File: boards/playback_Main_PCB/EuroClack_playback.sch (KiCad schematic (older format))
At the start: 31 parts

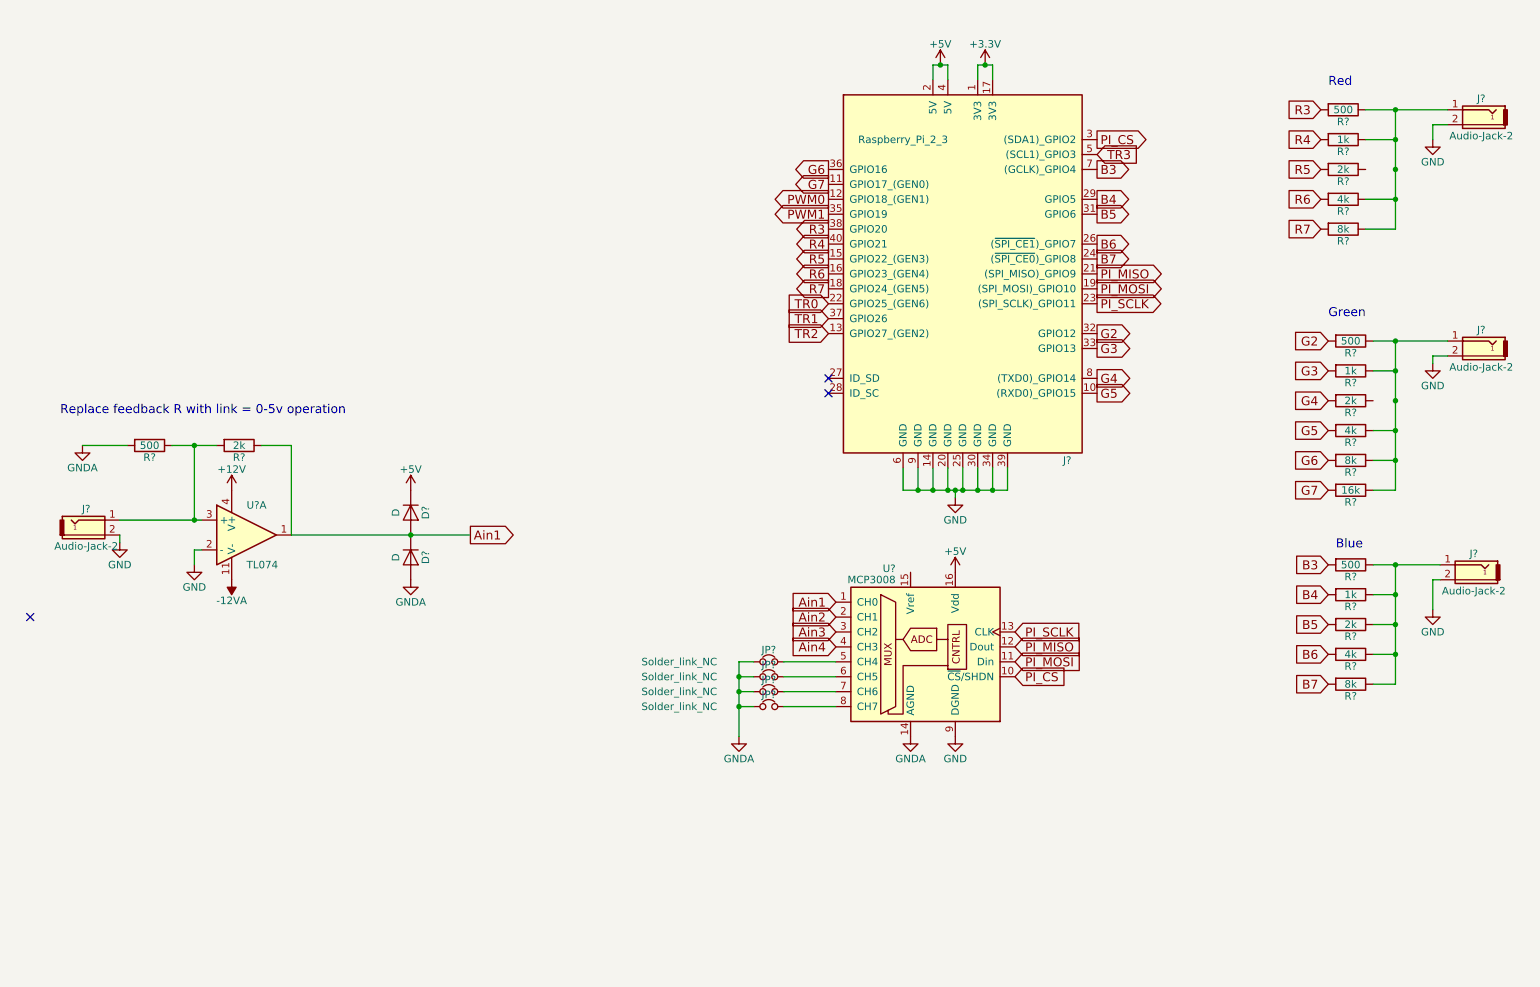
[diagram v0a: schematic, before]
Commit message: Added headers and started inputs
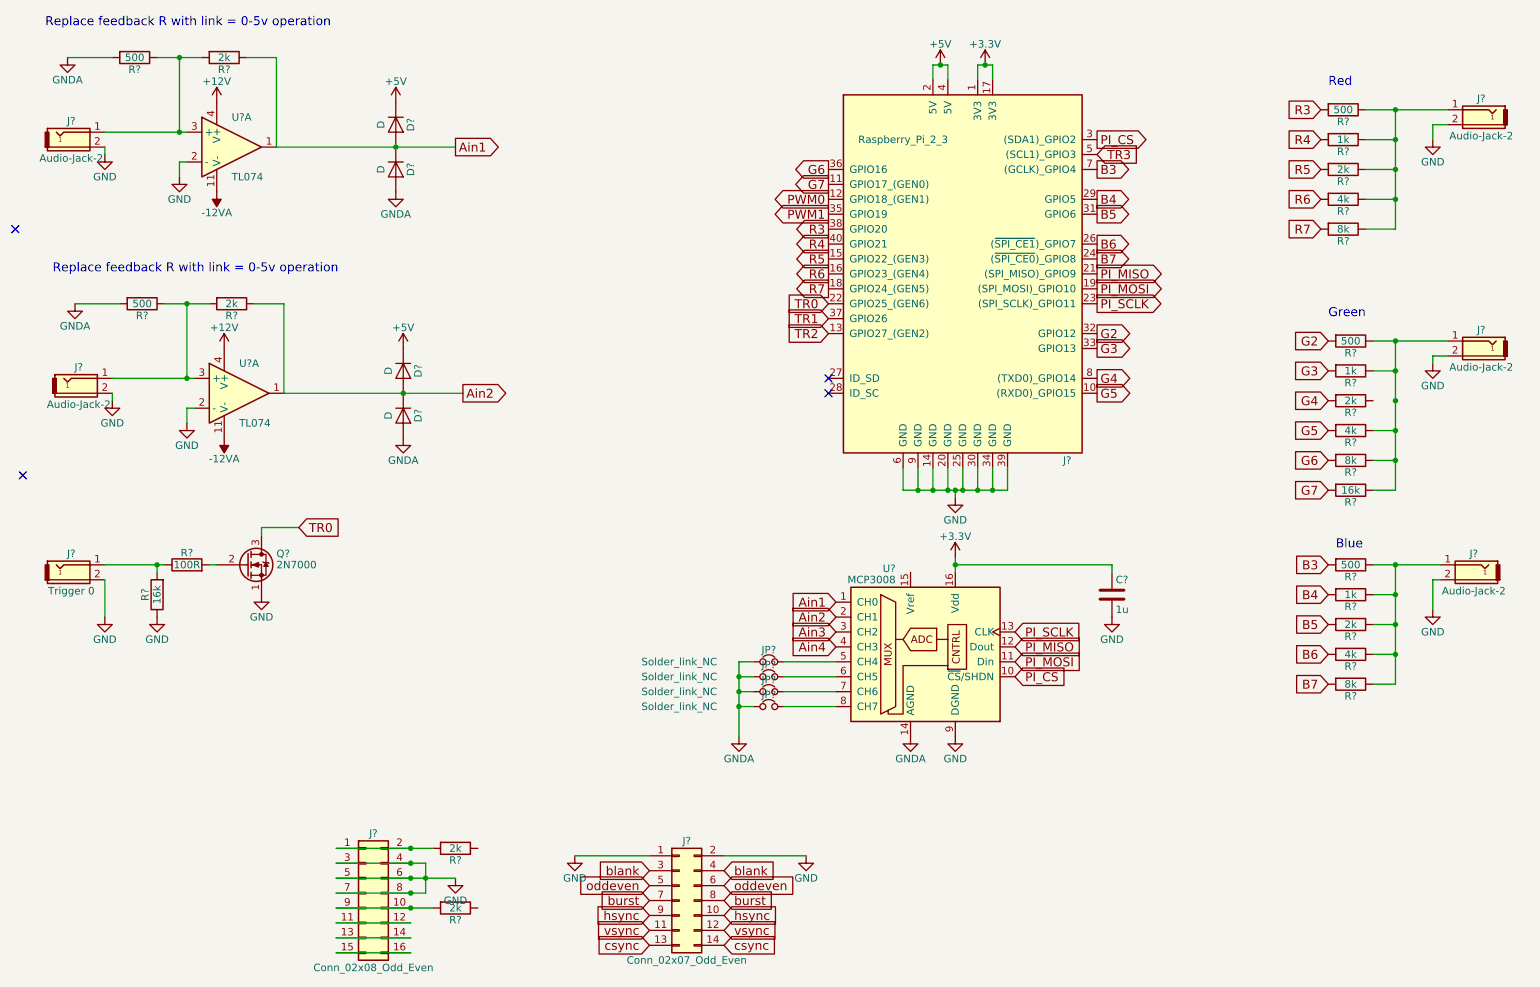
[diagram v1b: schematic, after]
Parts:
- added C?: 1u, symbol C
- added D? (x2): D, symbol D
- added J?: Conn_02x07_Odd_Even, symbol Conn_02x07_Odd_Even
- added J?: Conn_02x08_Odd_Even, symbol Conn_02x08_Odd_Even
- added J?: Audio-Jack-2, symbol Audio-Jack-2
- added J?: Trigger 0, symbol Audio-Jack-2
- added Q?: 2N7000, TO_SOT_Packages_THT:TO-92_Molded_Narrow, symbol 2N7000
- added R? (x3): 2k, symbol R
- added R?: 500, symbol R
- added R?: 16k, symbol R
- added R?: 100R, symbol R
- added U?: TL074, symbol TL074
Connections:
- net +12V: now also U?.4 (V+)
- net +3V3: now also U?.16 (Vdd), C?.1
- net +5V: now also D?.1 (K); no longer U?.16 (Vdd)
- net -12VA: now also U?.11 (V-)
- net Ain2: now also D?.1 (K), D?.2 (A), R?.1, U?.1
- net GND: now also C?.2, J?.1 (Pin_1), J?.2, J?.2, J?.2 (Pin_2), J?.3 (Pin_3), J?.4 (Pin_4), J?.5 (Pin_5), J?.6 (Pin_6), J?.7 (Pin_7), J?.8 (Pin_8), Q?.1 (S), R?.1, U?.2 (-)
- net GNDA: now also D?.2 (A), R?.2
- net TR0: now also Q?.3 (D)
- net at J?.1, R?.1, R?.1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: now also R?.1
- new net: J?.1 (Pin_1), J?.2 (Pin_2), R?.2
- new net: J?.10 (Pin_10), J?.9 (Pin_9), R?.2
- new net: J?.11 (Pin_11), J?.12 (Pin_12)
- new net: J?.13 (Pin_13), J?.14 (Pin_14)
- new net: J?.15 (Pin_15), J?.16 (Pin_16)
- new net: J?.1, R?.1, R?.2, U?.3 (+)
- new net: Q?.2 (G), R?.2
- new net: J?.1, R?.1, R?.2
- new net blank: J?.3 (Pin_3), J?.4 (Pin_4)
- new net burst: J?.7 (Pin_7), J?.8 (Pin_8)
- new net csync: J?.13 (Pin_13), J?.14 (Pin_14)
- new net hsync: J?.10 (Pin_10), J?.9 (Pin_9)
- new net oddeven: J?.5 (Pin_5), J?.6 (Pin_6)
- new net vsync: J?.11 (Pin_11), J?.12 (Pin_12)
- no-connect marks 3 -> 4
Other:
- moved on the sheet: D?, J?, R?, U?A
